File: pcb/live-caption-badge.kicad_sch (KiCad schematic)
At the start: 47 parts, among them J1 Conn_01x09, J2 Conn_01x06, J3 Conn_01x09, J5 USB_C_Receptacle_USB2.0_16P, SW1 SW_DPDT_x2, SW2 RST, SW3 BTN, SW4 BTN, SW5 BTN, SW6 RST, U1 ESP32-S3-WROOM-1, U2 HE9073A33M5R, U3 HE9073A33M5R

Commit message: pcb: Yippee
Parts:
- added R15: 1M, Resistor_SMD:R_0603_1608Metric, symbol Device:R_US
- added R16: 2M, Resistor_SMD:R_0603_1608Metric, symbol Device:R_US
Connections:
- net +BATT: now also R15.2
- net GND: now also R16.1
- net BATT_ADC: now reaches U1.15 (IO3)
- net BATT_ADC: now also R15.1, R16.2
- no-connect marks 17 -> 16
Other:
- moved on the sheet: D1, R6

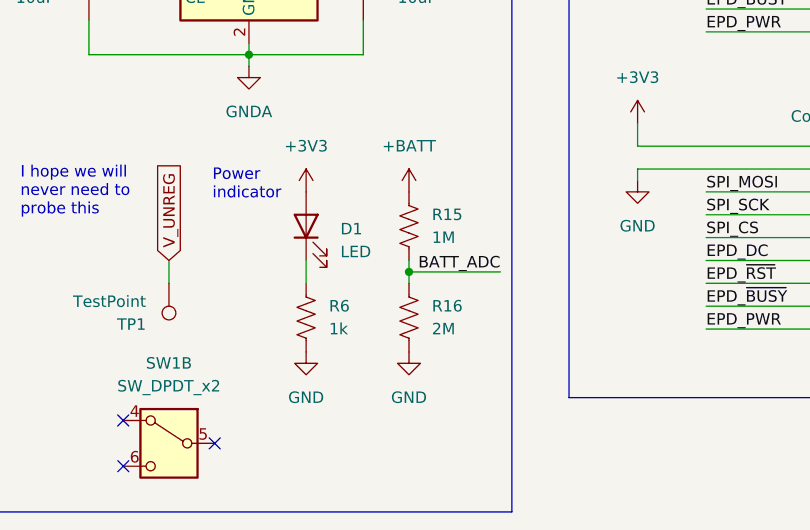
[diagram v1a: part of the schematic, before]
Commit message: pcb: Edit a couple R/C values, generate BOM
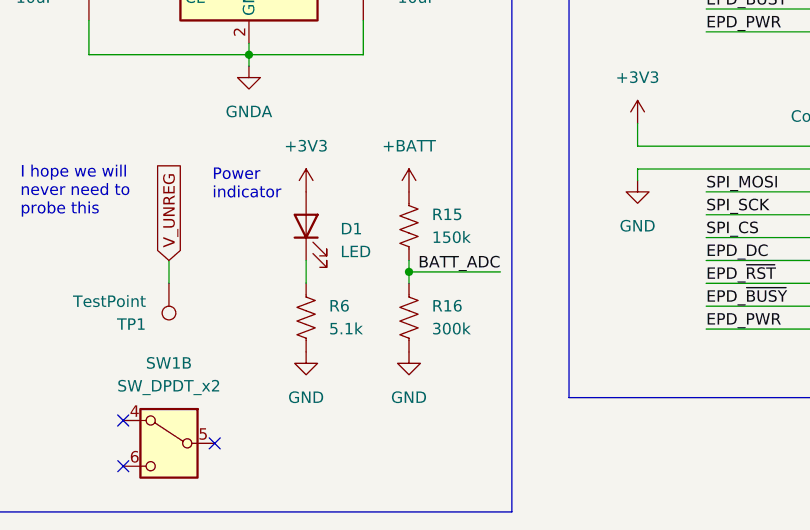
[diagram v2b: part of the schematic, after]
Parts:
- R15: value 1M -> 150k
- R16: value 2M -> 300k
- R6: value 1k -> 5.1k
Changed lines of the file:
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@@
 			)
 		)
-		(property "Value" "1M"
+		(property "Value" "150k"
 			(at 73.66 160.0199 0)
 			(effects
@@
 			)
 		)
-		(property "Value" "1k"
+		(property "Value" "5.1k"
 			(at 62.23 170.1799 0)
 			(effects
@@
 			)
 		)
-		(property "Value" "2M"
+		(property "Value" "300k"
 			(at 73.66 170.1799 0)
 			(effects

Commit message: pcb: Rev 2 schematic
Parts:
- removed J1: Conn_01x09, live-caption-badge:Molex_CLIK-Mate_502386-0970_1x09-1MP_P1.25mm_Horizontal, symbol Connector_Generic:Conn_01x09
- removed J3: Conn_01x09, Connector_PinHeader_2.54mm:PinHeader_1x09_P2.54mm_Vertical, symbol Connector_Generic:Conn_01x09
- added TP17: TestPoint, Connector_PinHeader_2.54mm:PinHeader_1x01_P2.54mm_Vertical, symbol Connector:TestPoint
- C1: footprint Capacitor_SMD:C_0603_1608Metric -> Capacitor_THT:CP_Radial_D8.0mm_P3.50mm
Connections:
- net GND: now also TP17.1
- net SPI_CS renamed SPI_~{CS}
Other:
- added sheet E-Paper (epaper.kicad_sch)
- note added: "Buttons"
- note added: "Use internal pull-up resistors"
- note removed: "E-Paper"
- note removed: "Generic buttons. Use internal pull-up resistors"
- moved on the sheet: C11, C12, C13, SW3, SW4, SW5, TP10, TP11, TP4, TP5, TP6, TP7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

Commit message: pcb: rev 2?
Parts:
- removed TP10, TP11, TP17, TP4, TP5, TP6, TP7, TP8, TP9: TestPoint, Connector_PinHeader_2.54mm:PinHeader_1x01_P2.54mm_Vertical, symbol Connector:TestPoint
- added Q2, Q3: SS8050, Package_TO_SOT_SMD:SOT-23, symbol Transistor_BJT:SS8050
- added R18, R19: 10k, Resistor_SMD:R_0603_1608Metric, symbol Device:R_US
- SW6: value RST -> FLASH
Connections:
- net EPD_DC: now also U1.21 (IO13); no longer U1.19 (IO11)
- net EPD_PWR: no longer U1.7 (IO7)
- net EPD_~{BUSY}: now also U1.19 (IO11); no longer U1.24 (IO47)
- net ESP_IO0: now also Q3.3 (C); no longer J2.4 (Pin_4)
- net SPI_MOSI: now also U1.24 (IO47); no longer U1.22 (IO14)
- net SPI_SCK: now also U1.23 (IO21); no longer U1.21 (IO13)
- net SPI_~{CS}: now also U1.22 (IO14); no longer U1.8 (IO15)
- net ESP_EN renamed ESP_~{EN}
- net ESP_~{EN}: now also Q2.3 (C); no longer J2.5 (Pin_5)
- new net: Q2.1 (B), Q3.2 (E), R18.1
- new net: Q2.2 (E), Q3.1 (B), R19.1
- new net UART_DTR: J2.5 (Pin_5), R18.2
- new net UART_RTS: J2.4 (Pin_4), R19.2
- no-connect marks 16 -> 17
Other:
- note added: "General purpose buttons"
- note removed: "Buttons"
- note removed: "I2S & I2C Testpoints"
- moved on the sheet: C1, C11, C12, C13, C2, C3, C4, C5, J2, J5, R1, R13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

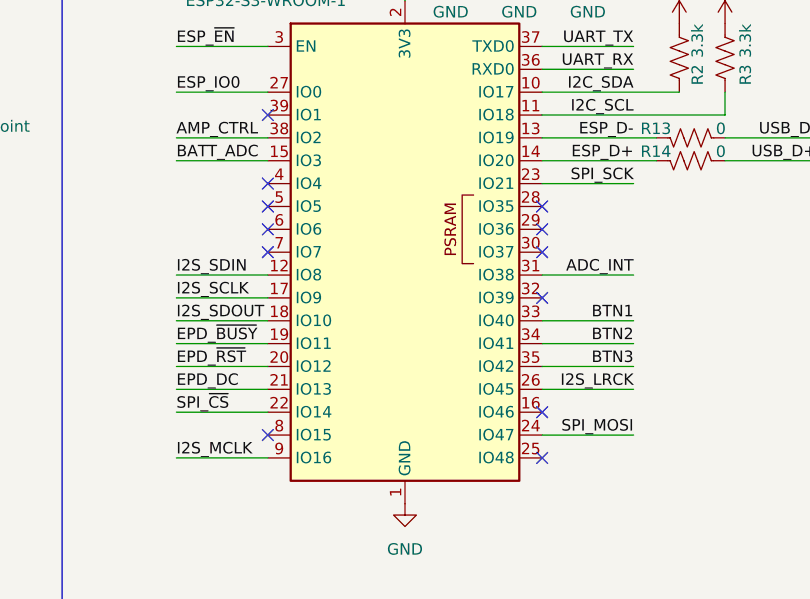
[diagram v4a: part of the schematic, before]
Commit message: pcb: Flip FPC, 170x105mm
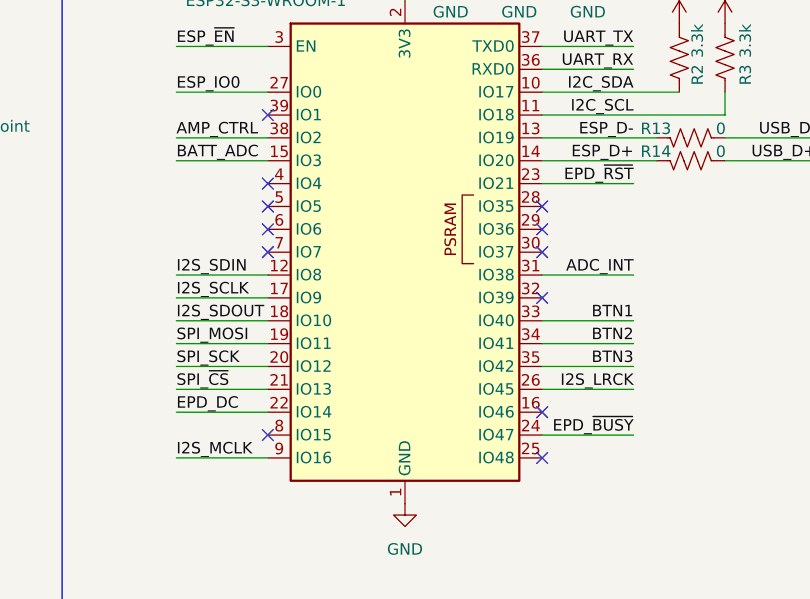
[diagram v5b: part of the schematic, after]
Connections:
- net EPD_DC: now also U1.22 (IO14); no longer U1.21 (IO13)
- net EPD_~{BUSY}: now also U1.24 (IO47); no longer U1.19 (IO11)
- net EPD_~{RST}: now also U1.23 (IO21); no longer U1.20 (IO12)
- net SPI_MOSI: now also U1.19 (IO11); no longer U1.24 (IO47)
- net SPI_SCK: now also U1.20 (IO12); no longer U1.23 (IO21)
- net SPI_~{CS}: now also U1.21 (IO13); no longer U1.22 (IO14)
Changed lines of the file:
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@@
 	)
 	(label "SPI_~{CS}"
-		(at 95.25 95.25 0)
+		(at 95.25 92.71 0)
 		(fields_autoplaced yes)
 		(effects
@@
 	)
 	(label "SPI_SCK"
-		(at 146.05 69.85 180)
-		(fields_autoplaced yes)
-		(effects
-			(font
-				(size 1.27 1.27)
-			)
-			(justify right bottom)
+		(at 95.25 90.17 0)
+		(fields_autoplaced yes)
+		(effects
+			(font
+				(size 1.27 1.27)
+			)
+			(justify left bottom)
 		)
 	)
@@
 	)
 	(label "EPD_~{BUSY}"
-		(at 95.25 87.63 0)
-		(fields_autoplaced yes)
-		(effects
-			(font
-				(size 1.27 1.27)
-			)
-			(justify left bottom)
+		(at 146.05 97.79 180)
+		(fields_autoplaced yes)
+		(effects
+			(font
+				(size 1.27 1.27)
+			)
+			(justify right bottom)
 		)
 	)
 	(label "EPD_DC"
-		(at 95.25 92.71 0)
+		(at 95.25 95.25 0)
 		(fields_autoplaced yes)
 		(effects
@@
 	)
 	(label "SPI_MOSI"
-		(at 146.05 97.79 180)
-		(fields_autoplaced yes)
-		(effects
-			(font
-				(size 1.27 1.27)
-			)
-			(justify right bottom)
+		(at 95.25 87.63 0)
+		(fields_autoplaced yes)
+		(effects
+			(font
+				(size 1.27 1.27)
+			)
+			(justify left bottom)
 		)
 	)
@@
 	)
 	(label "EPD_~{RST}"
-		(at 95.25 90.17 0)
-		(fields_autoplaced yes)
-		(effects
-			(font
-				(size 1.27 1.27)
-			)
-			(justify left bottom)
-		)
-	)
+		(at 146.05 69.85 180)
+		(fields_autoplaced yes)
+		(effects
+			(font
+				(size 1.27 1.27)
+			)
+			(justify right bottom)
+		)
+	)

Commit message: pcb: rev 2 ready?
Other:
- moved on the sheet: C4, C5, J2, Q2, Q3, R1, R18, R19, SW2, SW6

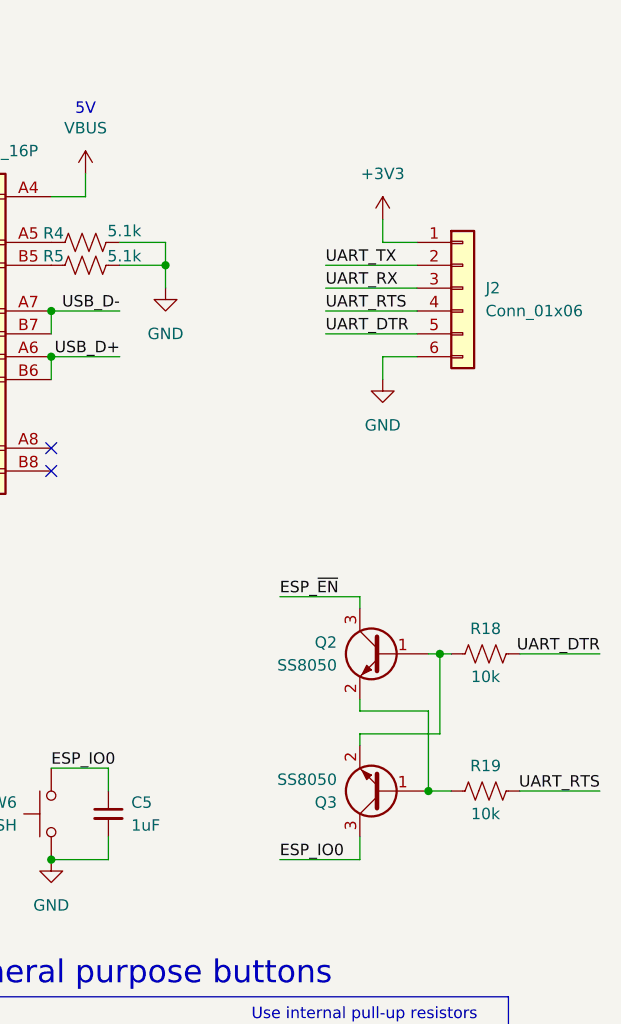
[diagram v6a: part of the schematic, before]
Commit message: pcb: Change paper size to US Letter
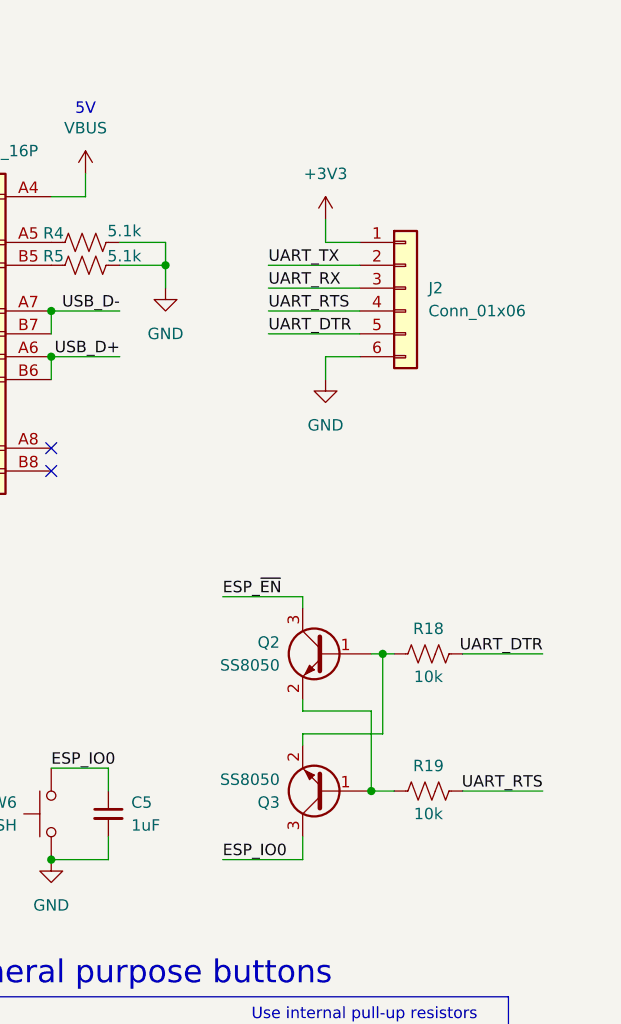
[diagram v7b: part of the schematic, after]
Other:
- moved on the sheet: J2, Q2, Q3, R18, R19
